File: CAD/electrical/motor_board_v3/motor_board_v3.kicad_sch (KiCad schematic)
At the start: 48 parts, among them J1 Conn_ST_STDC14, J2 12V, J3 I2C, J4 RS485, Q1 SI2301CDS-T1-GE3, U1 STM32F401RCTx, U2 MAX485E, U6 AMS1117-3.3, U8 SRV05-4, Y1 25MHz

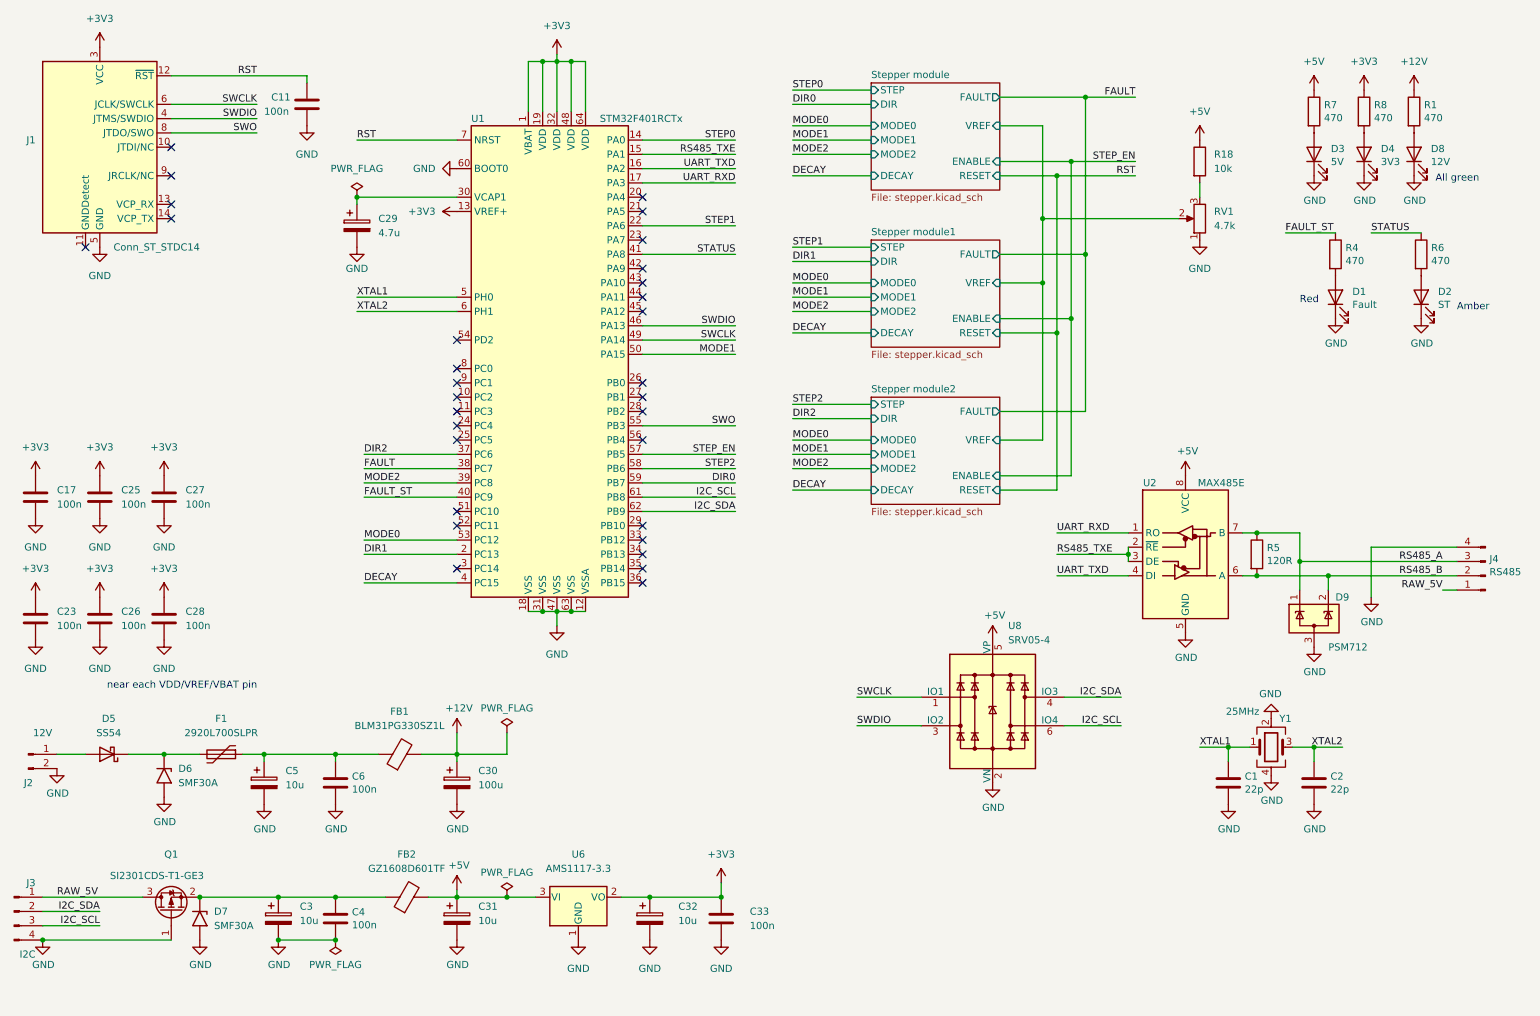
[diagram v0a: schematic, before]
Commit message: Updated version of motor board and main board (#3)
* Cleaning backup files

* [WIP] Main board V2

* [WIP] Implement RS485 in ultrasonic board

* Updated version of motor board and main board
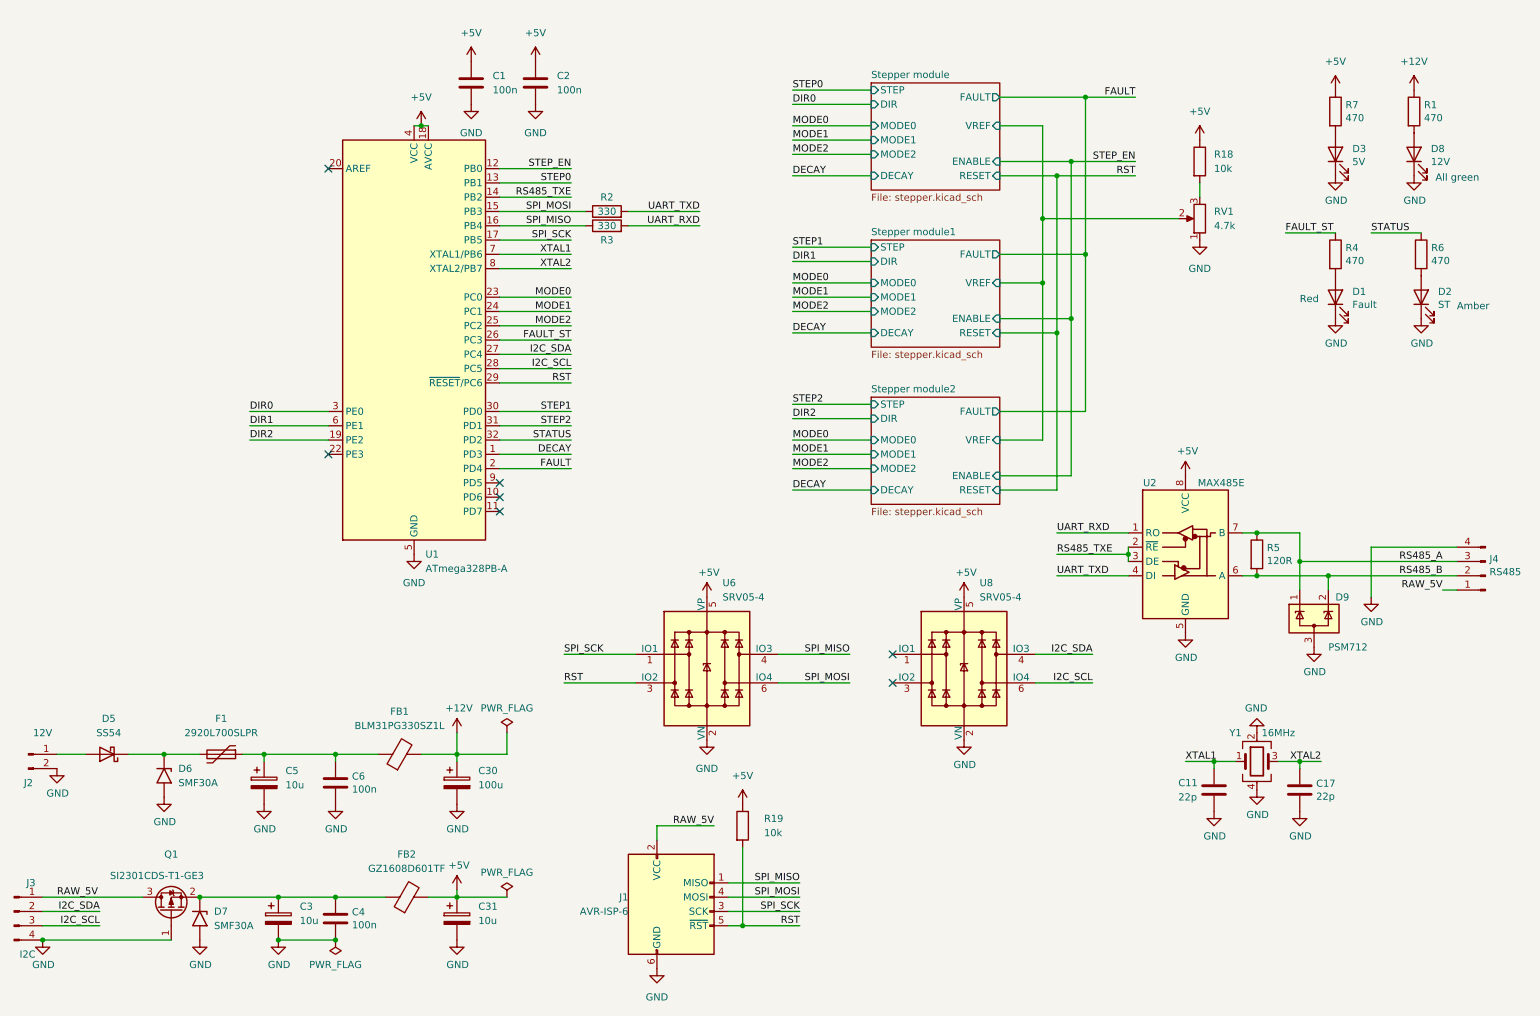
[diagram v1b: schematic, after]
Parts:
- removed C23, C25, C26, C27, C28, C33: 100n, Capacitor_SMD:C_0603_1608Metric, symbol Device:C
- removed C29: 4.7u, Capacitor_SMD:CP_Elec_5x5.4, symbol Device:C_Polarized
- removed C32: 10u, Capacitor_SMD:CP_Elec_5x5.4, symbol Device:C_Polarized
- removed D4: 3V3, LED_SMD:LED_0603_1608Metric, symbol Device:LED
- removed J1: Conn_ST_STDC14, Connector_PinHeader_1.27mm:PinHeader_2x07_P1.27mm_Vertical, symbol Connector:Conn_ST_STDC14
- removed R8: 470, Resistor_SMD:R_1206_3216Metric, symbol Device:R
- removed U1: STM32F401RCTx, Package_QFP:LQFP-64_10x10mm_P0.5mm, symbol MCU_ST_STM32F4:STM32F401RCTx
- removed U6: AMS1117-3.3, Package_TO_SOT_SMD:SOT-223-3_TabPin2, symbol Regulator_Linear:AMS1117-3.3
- added J1: AVR-ISP-6, Connector_PinHeader_2.54mm:PinHeader_2x03_P2.54mm_Vertical, symbol Connector:AVR-ISP-6
- added R19: 10k, Resistor_SMD:R_0603_1608Metric, symbol Device:R
- added R2, R3: 330, Resistor_SMD:R_0603_1608Metric, symbol Device:R
- added U1: ATmega328PB-A, Package_QFP:TQFP-32_7x7mm_P0.8mm, symbol MCU_Microchip_ATmega:ATmega328PB-A
- added U6: SRV05-4, Package_TO_SOT_SMD:SOT-23-6, symbol Power_Protection:SRV05-4
- C1, C2: value 22p -> 100n
- C11, C17: value 100n -> 22p
- C30: footprint Capacitor_SMD:CP_Elec_5x5.4 -> Capacitor_THT:CP_Radial_D10.0mm_P5.00mm
- Y1: value 25MHz -> 16MHz
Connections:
- net +3V3 is gone; now on net XTAL2: C17.1
- net +5V: now also C1.1, C2.1, R19.1, U1.18 (AVCC), U1.4 (VCC), U6.5 (VP)
- net DECAY: now also U1.1 (PD3)
- net DIR0: now also U1.3 (PE0)
- net DIR1: now also U1.6 (PE1)
- net DIR2: now also U1.19 (PE2)
- net FAULT: now also U1.2 (PD4)
- net FAULT_ST: now also U1.26 (PC3)
- net GND: now also J1.6 (GND), U1.21 (GND), U1.5 (GND), U6.2 (VN)
- net I2C_SCL: now also U1.28 (PC5)
- net I2C_SDA: now also U1.27 (PC4)
- net MODE0: now also U1.23 (PC0)
- net MODE1: now also U1.24 (PC1)
- net MODE2: now also U1.25 (PC2)
- net RAW_5V: now also J1.2 (VCC)
- net RS485_TXE: now also U1.14 (PB2)
- net RST: now also J1.5 (~{RST}), R19.2, U1.29 (~{RESET}/PC6), U6.3 (IO2); no longer C11.1
- net STATUS: now also U1.32 (PD2)
- net STEP0: now also U1.13 (PB1)
- net STEP1: now also U1.30 (PD0)
- net STEP2: now also U1.31 (PD1)
- net STEP_EN: now also U1.12 (PB0)
- net UART_RXD: now also R3.2
- net UART_TXD: now also R2.2
- net XTAL1: now also C11.1, U1.7 (XTAL1/PB6); no longer C1.1
- net XTAL2: now also U1.8 (XTAL2/PB7); no longer C2.1
- net SWCLK: no longer names the net of U8.1 (IO1)
- net SWDIO: no longer names the net of U8.3 (IO2)
- new net SPI_MISO: J1.1 (MISO), R3.1, U1.16 (PB4), U6.4 (IO3)
- new net SPI_MOSI: J1.4 (MOSI), R2.1, U1.15 (PB3), U6.6 (IO4)
- new net SPI_SCK: J1.3 (SCK), U1.17 (PB5), U6.1 (IO1)
- no-connect marks 31 -> 7
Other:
- note removed: "near each VDD/VREF/VBAT pin"
- moved on the sheet: D3, R7, U8
